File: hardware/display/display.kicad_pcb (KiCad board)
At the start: 2 copper layers, 110 x 70 mm, 8 parts, among them J1 Conn_02x03_Odd_Even

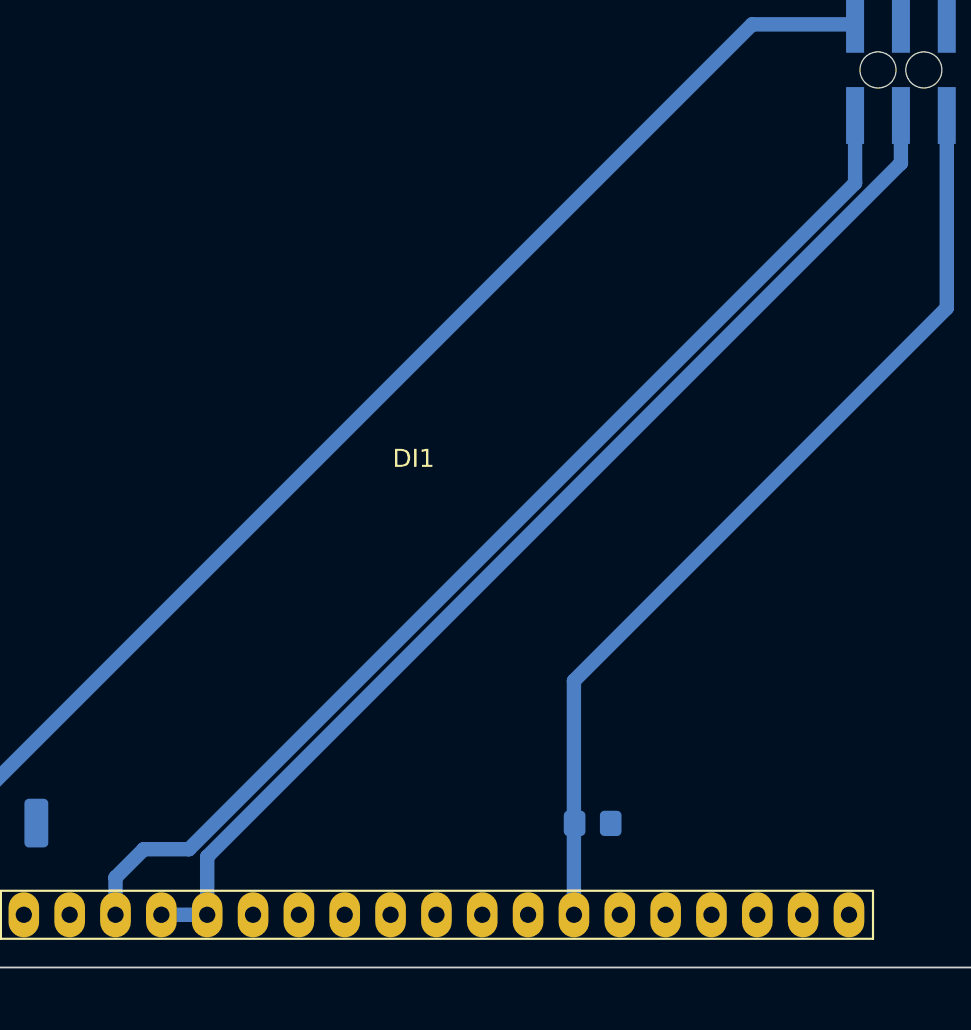
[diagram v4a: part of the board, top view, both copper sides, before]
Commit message: *: connect unused connectors pins to GND
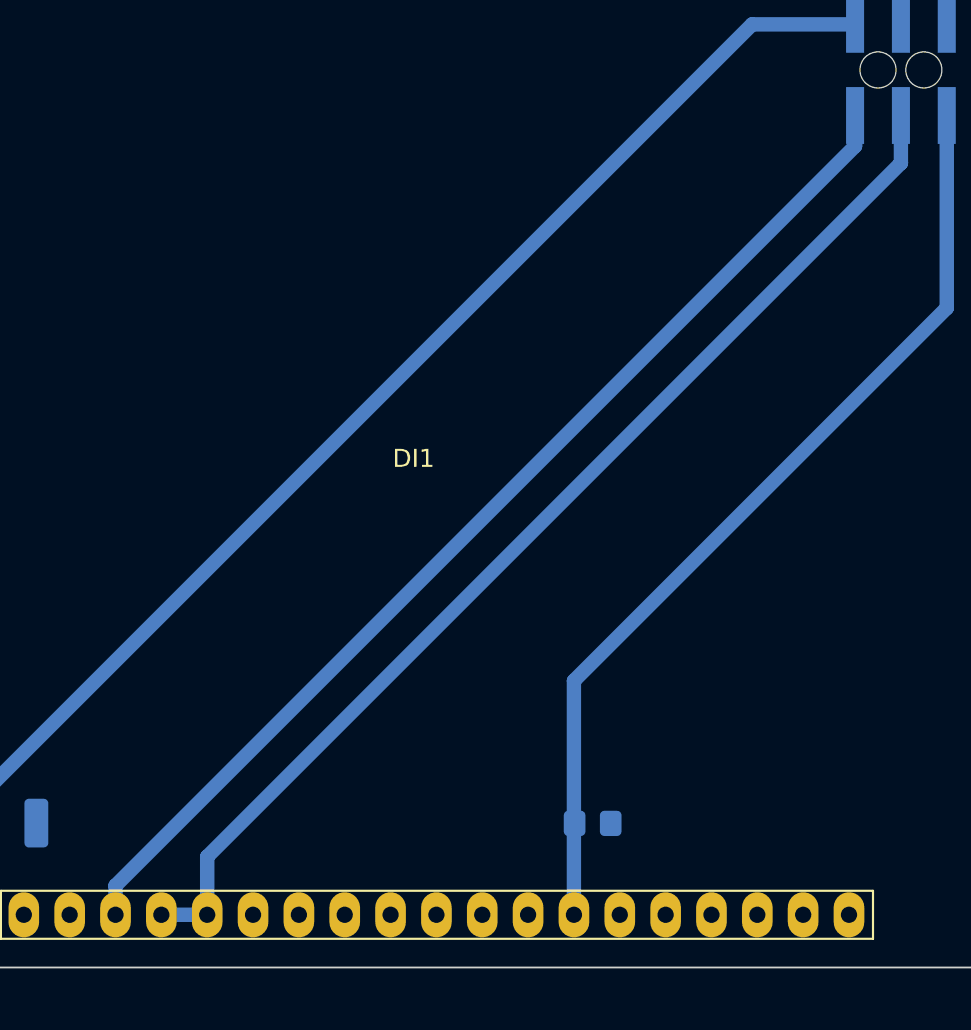
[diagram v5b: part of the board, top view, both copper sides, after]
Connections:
- J1 pad 2: unconnected-(J1-Pad2) -> GND
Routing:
- net /SCL: track 62.7 -> 61.3 mm
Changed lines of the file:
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@@
   (net 9 "/SDA")
   (net 10 "/~{RST_DISP}")
-  (net 11 "unconnected-(J1-Pad2)")
   (footprint "MountingHole:MountingHole_3.2mm_M3_DIN965_Pad" locked (layer "F.Cu")
     (at 155 145)
@@
       (net 2 "+5V") (pinfunction "Pin_1") (pintype "passive"))
     (pad "2" smd rect locked (at -2.525 0 270) (size 3.15 1) (layers "B.Cu" "B.Paste" "B.Mask")
-      (net 11 "unconnected-(J1-Pad2)") (pinfunction "Pin_2") (pintype "passive+no_connect"))
+      (net 1 "GND") (pinfunction "Pin_2") (pintype "passive"))
     (pad "3" smd rect locked (at -2.525 -2.54 270) (size 3.15 1) (layers "B.Cu" "B.Paste" "B.Mask")
       (net 1 "GND") (pinfunction "Pin_3") (pintype "passive"))
@@
   (segment (start 136.46 83.745) (end 130.755 83.745) (width 0.8) (layer "B.Cu") (net 2))
   (segment (start 88 126.5) (end 88 127.9625) (width 0.8) (layer "B.Cu") (net 2))
-  (segment (start 95.4825 131.0175) (end 95.4825 133.08) (width 0.8) (layer "B.Cu") (net 8))
-  (segment (start 97.0525 129.4475) (end 95.4825 131.0175) (width 0.8) (layer "B.Cu") (net 8))
-  (segment (start 136.46 88.795) (end 136.46 92.54) (width 0.8) (layer "B.Cu") (net 8))
-  (segment (start 136.46 92.54) (end 99.5525 129.4475) (width 0.8) (layer "B.Cu") (net 8))
-  (segment (start 99.5525 129.4475) (end 97.0525 129.4475) (width 0.8) (layer "B.Cu") (net 8))
+  (segment (start 136.46 88.795) (end 136.46 90.489) (width 0.8) (layer "B.Cu") (net 8))
+  (segment (start 95.4825 131.4665) (end 95.4825 133.08) (width 0.8) (layer "B.Cu") (net 8))
+  (segment (start 136.46 90.489) (end 95.4825 131.4665) (width 0.8) (layer "B.Cu") (net 8))
   (segment (start 139 91.428356) (end 100.5625 129.865856) (width 0.8) (layer "B.Cu") (net 9))
   (segment (start 100.5625 129.865856) (end 100.5625 133.08) (width 0.8) (layer "B.Cu") (net 9))

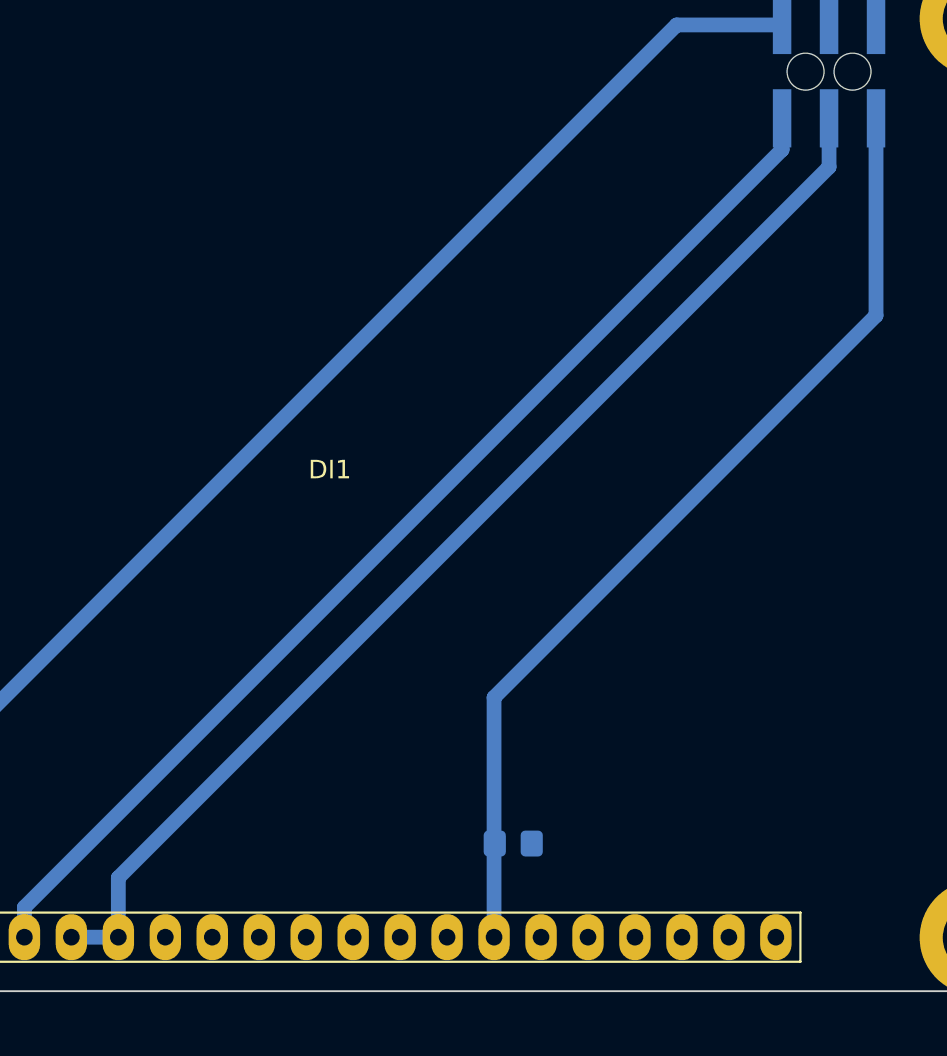
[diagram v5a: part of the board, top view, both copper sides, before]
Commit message: Increase clearance once again
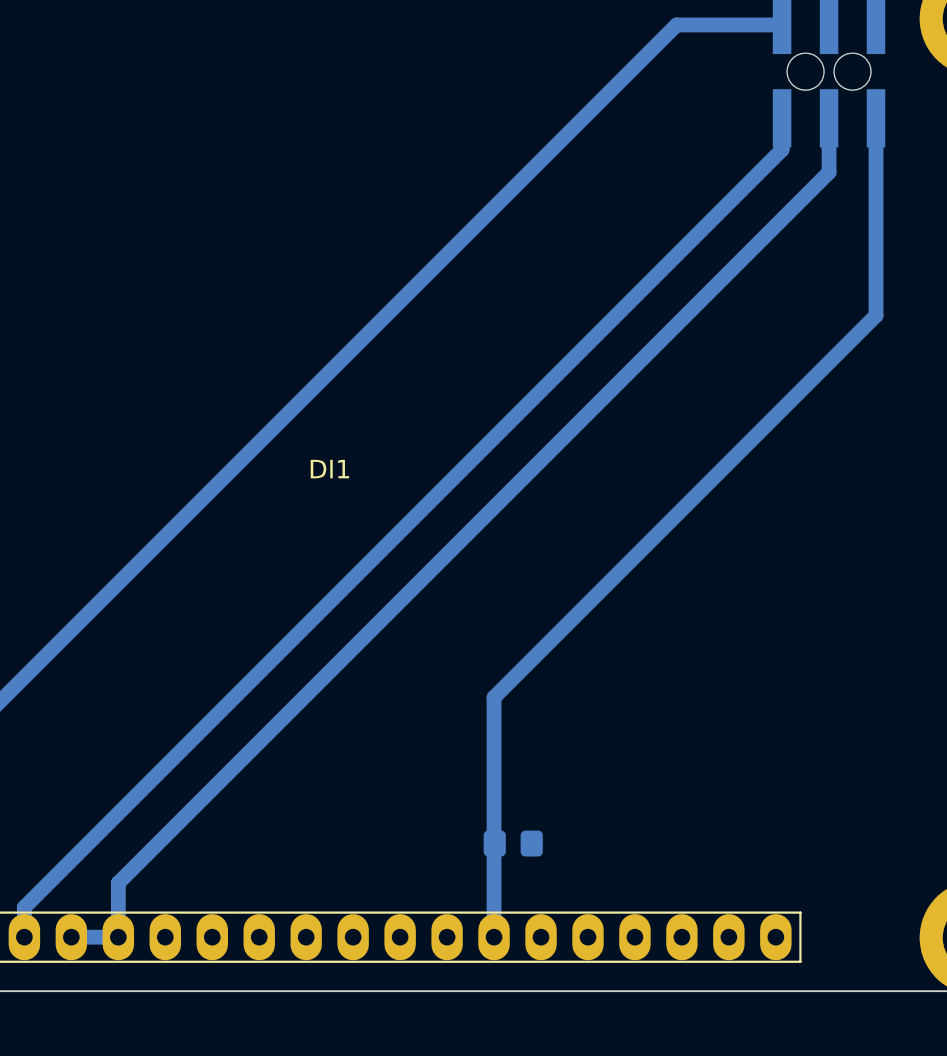
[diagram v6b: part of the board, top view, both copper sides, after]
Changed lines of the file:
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@@
   (segment (start 95.4825 131.4665) (end 95.4825 133.08) (width 0.8) (layer "B.Cu") (net 8))
   (segment (start 136.46 90.489) (end 95.4825 131.4665) (width 0.8) (layer "B.Cu") (net 8))
-  (segment (start 139 91.428356) (end 100.5625 129.865856) (width 0.8) (layer "B.Cu") (net 9))
-  (segment (start 100.5625 129.865856) (end 100.5625 133.08) (width 0.8) (layer "B.Cu") (net 9))
-  (segment (start 139 88.795) (end 139 91.428356) (width 0.8) (layer "B.Cu") (net 9))
+  (segment (start 139 88.795) (end 139 91.714178) (width 0.8) (layer "B.Cu") (net 9))
+  (segment (start 100.5625 130.151678) (end 100.5625 133.08) (width 0.8) (layer "B.Cu") (net 9))
+  (segment (start 139 91.714178) (end 100.5625 130.151678) (width 0.8) (layer "B.Cu") (net 9))
   (segment (start 98.0225 133.08) (end 100.5625 133.08) (width 0.8) (layer "B.Cu") (net 9))
   (segment (start 141.54 99.46) (end 120.8825 120.1175) (width 0.8) (layer "B.Cu") (net 10))
@@
   (segment (start 141.54 88.795) (end 141.54 99.46) (width 0.8) (layer "B.Cu") (net 10))
   (zone (net 1) (net_name "GND") (layer "B.Cu") (hatch edge 0.508)
-    (connect_pads (clearance 0.21))
+    (connect_pads (clearance 0.41))
     (min_thickness 0.254) (filled_areas_thickness no)
     (fill yes (thermal_gap 0.508) (thermal_bridge_width 0.508) (smoothing fillet) (radius 1))
